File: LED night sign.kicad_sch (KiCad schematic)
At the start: 38 parts, among them Q1 MOSFET-NCH-2N7002PW, Q2 BC817, U1 ATtiny85-20M, U2 APDS-9301

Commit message: enh schematic and added pdf
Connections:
- net INT: now also AC1.5 (INT)
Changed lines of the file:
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@@
+    (stroke (width 0) (type default) (color 0 0 0 0))
+  )
+  (wire (pts (xy 61.595 112.395) (xy 63.5 112.395))
     (stroke (width 0) (type default) (color 0 0 0 0))
   )
@@
     (property "Intersheet References" "${INTERSHEET_REFS}" (id 0) (at 201.531 34.8456 0)
       (effects (font (size 1.27 1.27)) (justify left) hide)
+    )
+  )
+  (global_label "INT" (shape output) (at 61.595 112.395 180) (fields_autoplaced)
+    (effects (font (size 1.27 1.27)) (justify right))
+    (property "Intersheet References" "${INTERSHEET_REFS}" (id 0) (at 56.279 112.3156 0)
+      (effects (font (size 1.27 1.27)) (justify right) hide)
     )
   )
@@
   (symbol (lib_id "SparkFun-DiscreteSemi:MOSFET-NCH-2N7002PW") (at 82.55 48.26 0) (unit 1)
     (in_bom yes) (on_board yes) (fields_autoplaced)
-    (property "Reference" "Q1" (id 0) (at 86.995 45.72 0)
+    (property "Reference" "Q1" (id 0) (at 87.63 46.99 0)
       (effects (font (size 1.143 1.143)) (justify left))
     )
-    (property "Value" "MOSFET-NCH-2N7002PW" (id 1) (at 86.995 48.26 0)
+    (property "Value" "MOSFET-NCH-2N7002PW" (id 1) (at 87.63 49.53 0)
       (effects (font (size 1.143 1.143)) (justify left))
     )
@@
     )
     (property "Field4" "TRANS-11151" (id 4) (at 86.995 51.435 0)
-      (effects (font (size 1.524 1.524)) (justify left))
-    )
-    (pin "1")
+      (effects (font (size 1.524 1.524)) (justify left) hide)
+    )
+    (pin "1")

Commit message: enh pcb and sch
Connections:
- net +3V0: no longer AC1.11 (IO_VDD_2), AC1.3 (IO_VDD_1), C1.1, C2.1, C3.1, C4.1, C5.1, R1.1, R2.2, TP8.1, U1.15 (VCC), U2.1 (VDD)
- net JouleThiefPWR: now also AC1.11 (IO_VDD_2), AC1.3 (IO_VDD_1), C1.1, C2.1, C3.1, C4.1, C5.1, R1.1, R2.2, TP8.1, U1.15 (VCC), U2.1 (VDD)
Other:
- note added: "Power Source"
- note removed: "Power"

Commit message: Improved pcb wiring
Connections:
- net INT renamed INTL
- net INTL: no longer AC1.5 (INT)
- net PB3 renamed INTM
- net INTM: now also AC1.5 (INT)
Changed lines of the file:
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@@
     (stroke (width 0) (type default) (color 0 0 0 0))
   )
-  (text "LEDS\n" (at 63.5 16.51 0)
+  (text "LEDS\n" (at 63.5 15.875 0)
     (effects (font (size 1.27 1.27)) (justify left bottom))
   )
@@
     (effects (font (size 1.27 1.27)) (justify left bottom))
   )
-  (text "Power Source\n\n\n" (at 250.19 75.565 0)
+  (text "Power Source\n\n\n" (at 250.19 76.2 0)
     (effects (font (size 1.27 1.27)) (justify left bottom))
   )
@@
     )
   )
-  (global_label "INT" (shape input) (at 146.685 32.385 180) (fields_autoplaced)
+  (global_label "INTL" (shape input) (at 146.685 32.385 180) (fields_autoplaced)
     (effects (font (size 1.27 1.27)) (justify right))
-    (property "Intersheet References" "${INTERSHEET_REFS}" (id 0) (at 141.369 32.3056 0)
+    (property "Intersheet References" "${INTERSHEET_REFS}" (id 0) (at 140.3409 32.3056 0)
       (effects (font (size 1.27 1.27)) (justify right) hide)
     )
@@
     )
   )
+  (global_label "INTM" (shape input) (at 146.685 34.925 180) (fields_autoplaced)
+    (effects (font (size 1.27 1.27)) (justify right))
+    (property "Intersheet References" "${INTERSHEET_REFS}" (id 0) (at 139.9176 34.8456 0)
+      (effects (font (size 1.27 1.27)) (justify right) hide)
+    )
+  )
   (global_label "PB4" (shape input) (at 146.685 37.465 180) (fields_autoplaced)
     (effects (font (size 1.27 1.27)) (justify right))
@@
     )
   )
-  (global_label "INT" (shape output) (at 61.595 112.395 180) (fields_autoplaced)
+  (global_label "INTM" (shape output) (at 61.595 112.395 180) (fields_autoplaced)
     (effects (font (size 1.27 1.27)) (justify right))
-    (property "Intersheet References" "${INTERSHEET_REFS}" (id 0) (at 56.279 112.3156 0)
+    (property "Intersheet References" "${INTERSHEET_REFS}" (id 0) (at 54.8276 112.3156 0)
       (effects (font (size 1.27 1.27)) (justify right) hide)
     )
@@
     )
   )
-  (global_label "INT" (shape output) (at 190.5 98.425 0) (fields_autoplaced)
+  (global_label "INTL" (shape output) (at 190.5 98.425 0) (fields_autoplaced)
     (effects (font (size 1.27 1.27)) (justify left))
-    (property "Intersheet References" "${INTERSHEET_REFS}" (id 0) (at 195.816 98.3456 0)
+    (property "Intersheet References" "${INTERSHEET_REFS}" (id 0) (at 196.8441 98.3456 0)
       (effects (font (size 1.27 1.27)) (justify left) hide)
     )
@@
     )
   )
-  (global_label "PB3" (shape input) (at 146.685 34.925 180) (fields_autoplaced)
-    (effects (font (size 1.27 1.27)) (justify right))
-    (property "Intersheet References" "${INTERSHEET_REFS}" (id 0) (at 140.5224 34.8456 0)
-      (effects (font (size 1.27 1.27)) (justify right) hide)
-    )
-  )

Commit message: changed ic for light sensing
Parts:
- removed U2: APDS-9301, OptoDevice:Broadcom_APDS-9301, symbol Sensor_Optical:APDS-9301
- added IC1: TSL25911FN, SamacSys_Parts:TSL25911FN, symbol SamacSys_Parts:TSL25911FN
- renumbered TP5 to GND1, TP1 to PB0, TP7 to PB1, TP6 to PB2, TP4 to PB3, TP3 to PB4, TP2 to PB5, TP8 to VCC1
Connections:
- net GND: now also IC1.3 (GND)
- net INTL: now also IC1.2 (INT)
- net JouleThiefPWR: now also IC1.5 (VDD)
- net PB0/SDA/MOSI: now also IC1.6 (SDA)
- net PB2/SCL/SCK: now also IC1.1 (SCL)

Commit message: Improved design and added 3D models
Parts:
- C1, C6: value 0.1uF -> 100nF
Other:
- moved on the sheet: L1

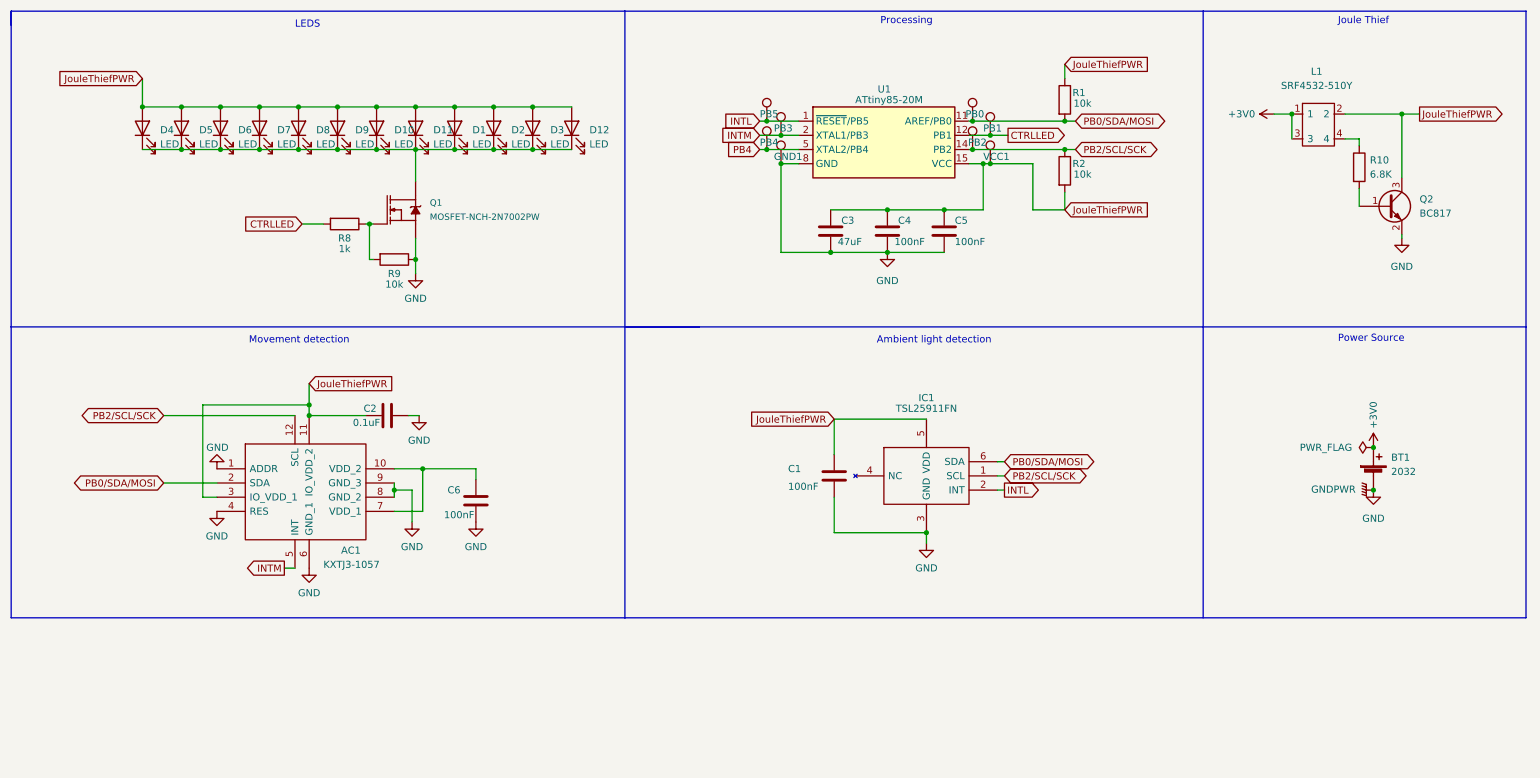
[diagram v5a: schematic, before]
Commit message: component placement done and starting wiring
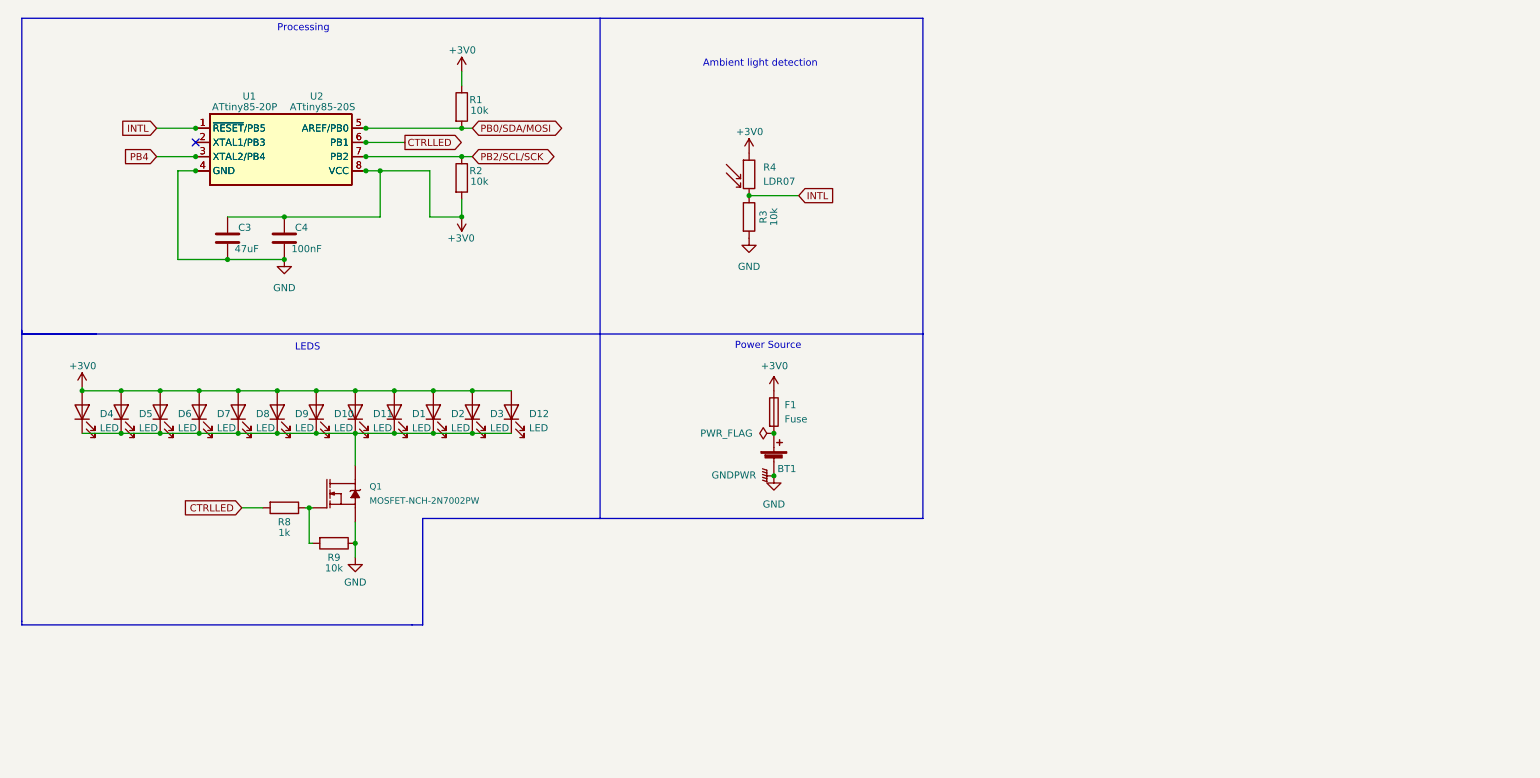
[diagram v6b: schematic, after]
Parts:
- removed AC1: KXTJ3-1057, SamacSys_Parts:2X2X0.9MMLGA, symbol SamacSys_Parts:KXTJ3-1057
- removed C1, C5, C6: 100nF, Capacitor_SMD:C_1206_3216Metric_Pad1.33x1.80mm_HandSolder, symbol Device:C
- removed C2: 0.1uF, Capacitor_SMD:C_1206_3216Metric_Pad1.33x1.80mm_HandSolder, symbol Device:C
- removed GND1: gnd, TestPoint:TestPoint_Pad_D1.0mm, symbol Connector:TestPoint
- removed IC1: TSL25911FN, SamacSys_Parts:TSL25911FN, symbol SamacSys_Parts:TSL25911FN
- removed L1: SRF4532-510Y, SamacSys_Parts:SRF4532220Y, symbol SamacSys_Parts:SRF4532-510Y
- removed PB0, PB3: pb0, TestPoint:TestPoint_Pad_D1.0mm, symbol Connector:TestPoint
- removed PB1: pb1, TestPoint:TestPoint_Pad_D1.0mm, symbol Connector:TestPoint
- removed PB2: pb2, TestPoint:TestPoint_Pad_D1.0mm, symbol Connector:TestPoint
- removed PB4: pb4, TestPoint:TestPoint_Pad_D1.0mm, symbol Connector:TestPoint
- removed PB5: pb5, TestPoint:TestPoint_Pad_D1.0mm, symbol Connector:TestPoint
- removed Q2: BC817, Package_TO_SOT_SMD:SOT-23, symbol Transistor_BJT:BC817
- removed R10: 6.8K, Resistor_SMD:R_1206_3216Metric_Pad1.30x1.75mm_HandSolder, symbol Device:R
- removed U1: ATtiny85-20M, SamacSys_Parts:QFN50P400X400X80-21N-D, symbol MCU_Microchip_ATtiny:ATtiny85-20M
- removed VCC1: vcc, TestPoint:TestPoint_Pad_D1.0mm, symbol Connector:TestPoint
- added F1: Fuse, Resistor_SMD:R_1206_3216Metric_Pad1.30x1.75mm_HandSolder, symbol Device:Fuse
- added R3: 10k, Resistor_SMD:R_1206_3216Metric_Pad1.30x1.75mm_HandSolder, symbol Device:R
- added R4: LDR07, OptoDevice:R_LDR_5.1x4.3mm_P3.4mm_Vertical, symbol Sensor_Optical:LDR07
- added U1: ATtiny85-20P, SamacSys_Parts:DIP781W56P254L950H533Q8N, symbol MCU_Microchip_ATtiny:ATtiny85-20P
- added U2: ATtiny85-20S, Package_SO:SOIC-8W_5.3x5.3mm_P1.27mm, symbol MCU_Microchip_ATtiny:ATtiny85-20S
- BT1: footprint SamacSys_Parts:SMTU2032LF -> Battery:BatteryHolder_Keystone_3002_1x2032
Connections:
- net JouleThiefPWR is gone; now on net +3V0: C3.1, C4.1, D1.2 (A), D10.2 (A), D11.2 (A), D12.2 (A), D2.2 (A), D3.2 (A), D4.2 (A), D5.2 (A), D6.2 (A), D7.2 (A), D8.2 (A), D9.2 (A), R1.1, R2.2
- net +3V0: now also F1.1, R4.1, U1.8 (VCC), U2.8 (VCC); no longer BT1.1 (+)
- net CTRLLED: now also U1.6 (PB1), U2.6 (PB1)
- net GND: now also R3.2, U1.4 (GND), U2.4 (GND)
- net INTL: now also R3.1, R4.2, U1.1 (~{RESET}/PB5), U2.1 (~{RESET}/PB5)
- net PB0/SDA/MOSI: now also U1.5 (AREF/PB0), U2.5 (AREF/PB0)
- net PB2/SCL/SCK: now also U1.7 (PB2), U2.7 (PB2)
- net PB4: now also U1.3 (XTAL2/PB4), U2.3 (XTAL2/PB4)
- new net: BT1.1 (+), F1.2
- new net: U1.2 (XTAL1/PB3), U2.2 (XTAL1/PB3)
- no-connect marks 0 -> 1
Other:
- note removed: "Joule Thief"
- note removed: "Movement detection"
- moved on the sheet: C3, C4, D1, D10, D11, D12, D2, D3, D4, D5, D6, D7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

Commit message: added push button
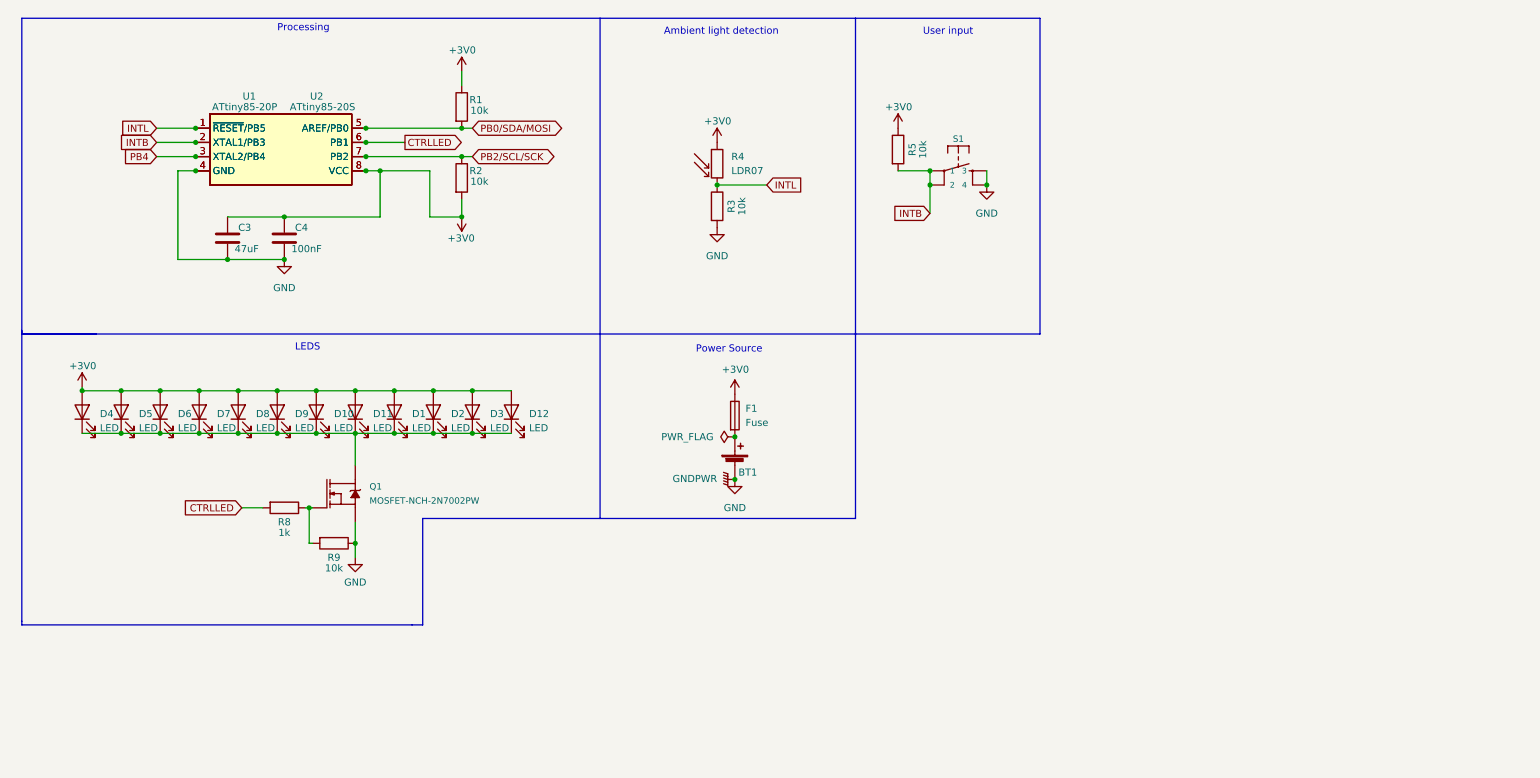
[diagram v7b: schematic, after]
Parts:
- added R5: 10k, Resistor_SMD:R_1206_3216Metric_Pad1.30x1.75mm_HandSolder, symbol Device:R
- added S1: MOMENTARY-SWITCH-SPST-2-SMD-5.2MM, Button_Switch_SMD:SW_SPST_TL3305B, symbol SparkFun-Switches:MOMENTARY-SWITCH-SPST-2-SMD-5.2MM
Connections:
- net +3V0: now also R5.1
- net GND: now also S1.3, S1.4
- net INTB: now reaches U1.2 (XTAL1/PB3), U2.2 (XTAL1/PB3)
- net INTB: now also R5.2, S1.1, S1.2
- no-connect marks 1 -> 0
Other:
- note added: "User input"
- moved on the sheet: BT1, F1, R3, R4

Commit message: added mounting hole (for keychain)
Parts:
- added H1: MountingHole, MountingHole:MountingHole_2.5mm, symbol Mechanical:MountingHole
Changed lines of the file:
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@@
     (pin "2")
+  )
+  (symbol (lib_id "Mechanical:MountingHole") (at 196.215 145.415 0) (unit 1)
+    (in_bom yes) (on_board yes) (fields_autoplaced)
+    (property "Reference" "H1" (id 0) (at 199.39 144.1449 0)
+      (effects (font (size 1.27 1.27)) (justify left))
+    )
+    (property "Value" "MountingHole" (id 1) (at 199.39 146.6849 0)
+      (effects (font (size 1.27 1.27)) (justify left))
+    )
+    (property "Footprint" "MountingHole:MountingHole_2.5mm" (id 2) (at 196.215 145.415 0)
+      (effects (font (size 1.27 1.27)) hide)
+    )
+    (property "Datasheet" "~" (id 3) (at 196.215 145.415 0)
+      (effects (font (size 1.27 1.27)) hide)
+    )
   )
   (symbol (lib_id "Device:R") (at 93.345 29.845 0) (unit 1)
@@
       (reference "F1") (unit 1) (value "Fuse") (footprint "Resistor_SMD:R_1206_3216Metric_Pad1.30x1.75mm_HandSolder")
     )
+    (path "/18aaa3d5-9221-4b3f-8be5-2310d7570018"
+      (reference "H1") (unit 1) (value "MountingHole") (footprint "MountingHole:MountingHole_2.5mm")
+    )
     (path "/4db6fdb1-7f8f-4325-b408-7754347a443b"
